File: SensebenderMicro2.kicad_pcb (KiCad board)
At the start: 2 copper layers, 18.7 x 30.5 mm, 31 parts, among them P1 Debug, P2 MYSX_1.2, P3 Antenna, U1 ATSAMD21E, U2 AP1117D33, U3 NRF24L01, U4 RFM69HW, U5 ATSHA204A, U6 AT25DF512C, U7 Si7021, U8 AT24C32-STUM-T, Y1 32Khz

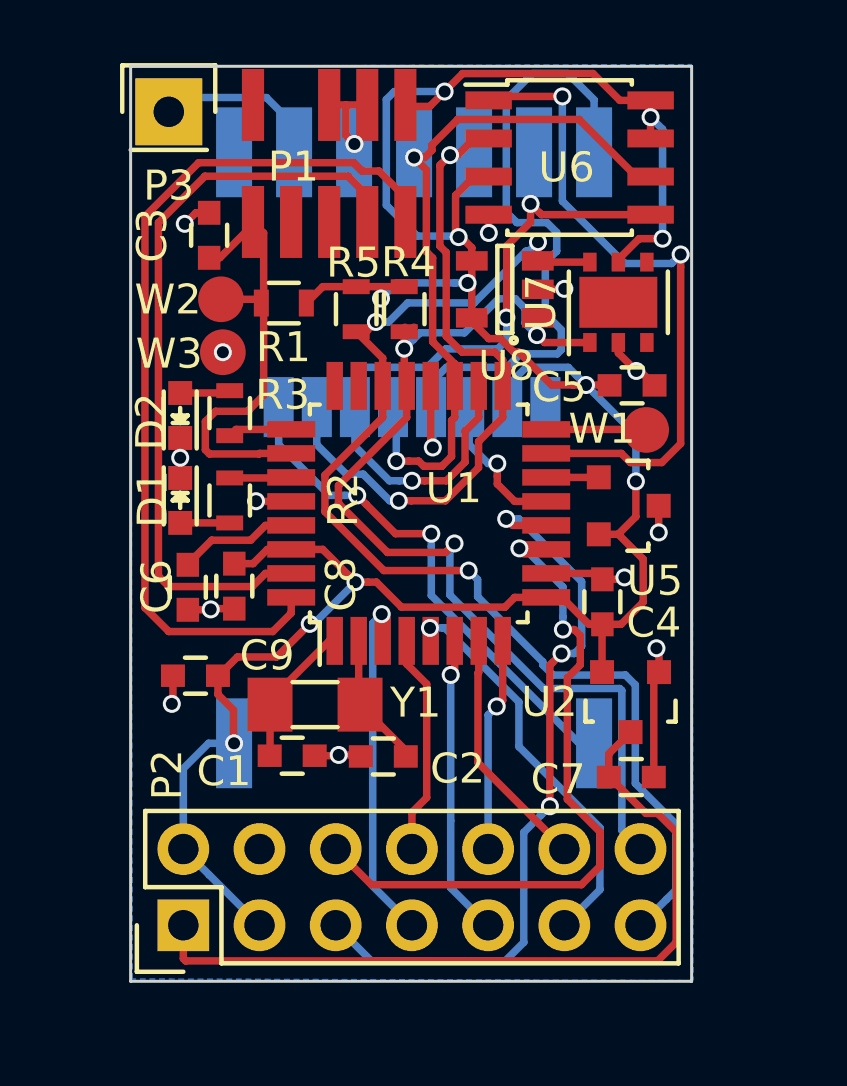
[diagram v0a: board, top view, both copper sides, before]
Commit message: Added filtering for analog supply
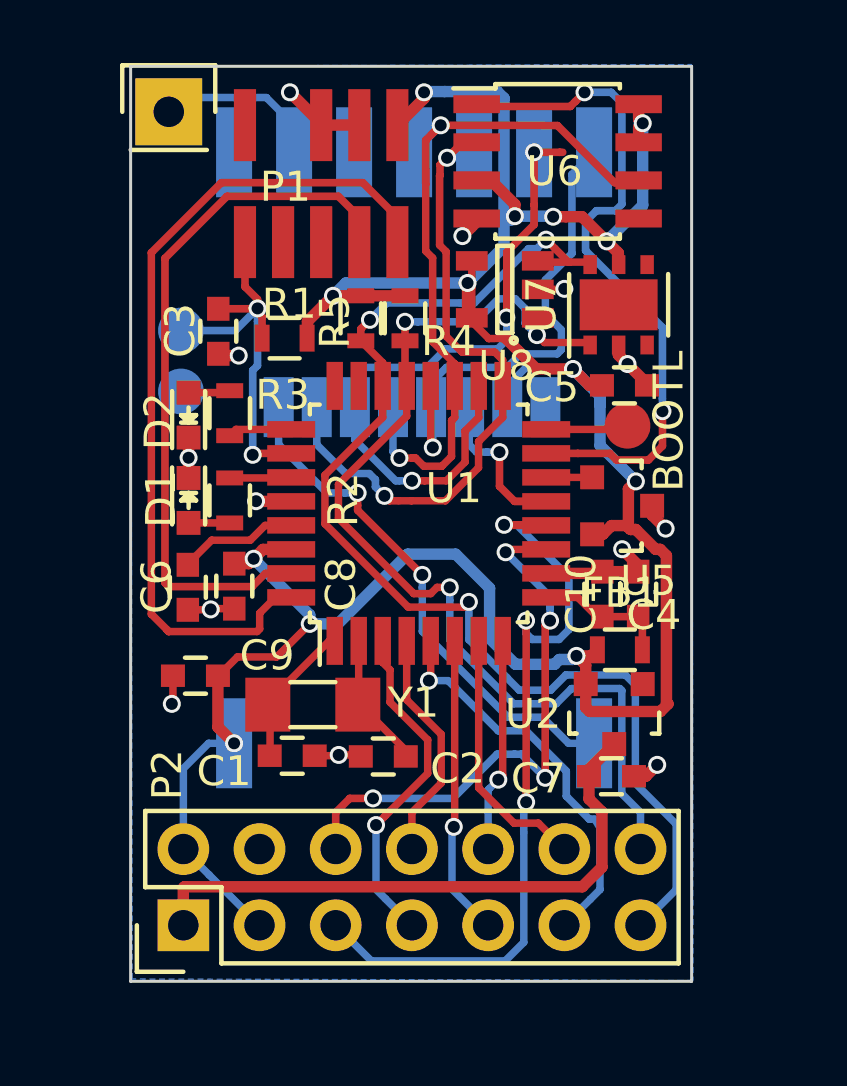
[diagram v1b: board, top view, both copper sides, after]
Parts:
- added C10: CP, Capacitors_SMD:C_0603, F.Cu at (105.9, 99.7)
- added FB1: FILTER, Resistors_SMD:R_0603, F.Cu at (105.3, 101.5)
- added REF**: Symbol_OSHW-Logo_SilkScreen, Symbols:Symbol_OSHW-Logo_SilkScreen, B.Cu at (98.8, 102.5)
- U2: value AP1117D33 -> MCP1703T-3302E
- W2, W3: moved to B.Cu
- moved C3 3.21 mm to (91.9, 90.9), turned to 270 degrees
- moved W3 1.91 mm to (90.7, 92.9)
- moved W2 1.69 mm to (90.7, 90.9)
- moved R1 1.17 mm to (94.1, 91.2)
- moved P1 0.72 mm to (95.4, 86.0)
- moved U2 0.67 mm to (105.1, 103.7)
- moved C7 0.66 mm to (105.0, 105.8)
- moved W1 0.64 mm to (105.6, 94.1)
- moved U6 0.42 mm to (103.2, 85.3)
- moved R5 0.34 mm to (96.7, 90.5)
- moved R4 0.31 mm to (98.1, 90.5)
- moved D2 0.28 mm to (90.9, 93.7)
- moved D1 0.28 mm to (90.9, 96.6)
- moved C4 0.25 mm to (104.7, 99.7)
- moved C5 0.25 mm to (105.5, 92.7)
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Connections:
- net Net-(U4-Pad1) renamed /RFM_RESET
- C4 pad 2: +3V3 -> Net-(C10-Pad1)
- U1 pad 9: +3V3 -> Net-(C10-Pad1)
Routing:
- net /CSN: track 24.5 -> 17.1 mm
- net +3V3: track 89.7 -> 97.0 mm, vias 11 -> 13
- net /V_RAW: track 26.3 -> 20.7 mm
- net Net-(C10-Pad1): track 0.00 -> 4.65 mm
- net /D2_DTM: track 22.8 -> 19.0 mm, vias 2 -> 4
- net /MOSI: track 26.1 -> 23.1 mm
- net /NRF_CE: track 5.00 -> 7.67 mm
- net /D1_DFM: track 24.9 -> 27.0 mm
- net /D7_SCL: track 38.8 -> 40.7 mm
- net /RESET: track 15.6 -> 13.9 mm, vias 0 -> 2
- net /SCK: track 24.1 -> 25.8 mm
- net /SWCLK: track 25.4 -> 23.7 mm
- net /SWDIO: track 29.8 -> 28.3 mm
- net /A1: track 11.9 -> 11.3 mm
- net GND: track 22.2 -> 21.8 mm, vias 14 -> 13
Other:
- net class Default: trace_width 0.25 -> 0.254
- net class power added: clearance 0.2, trace_width 0.381, via_dia 0.6, via_drill 0.4

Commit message: Added fet to switch power to radio / ATSHA
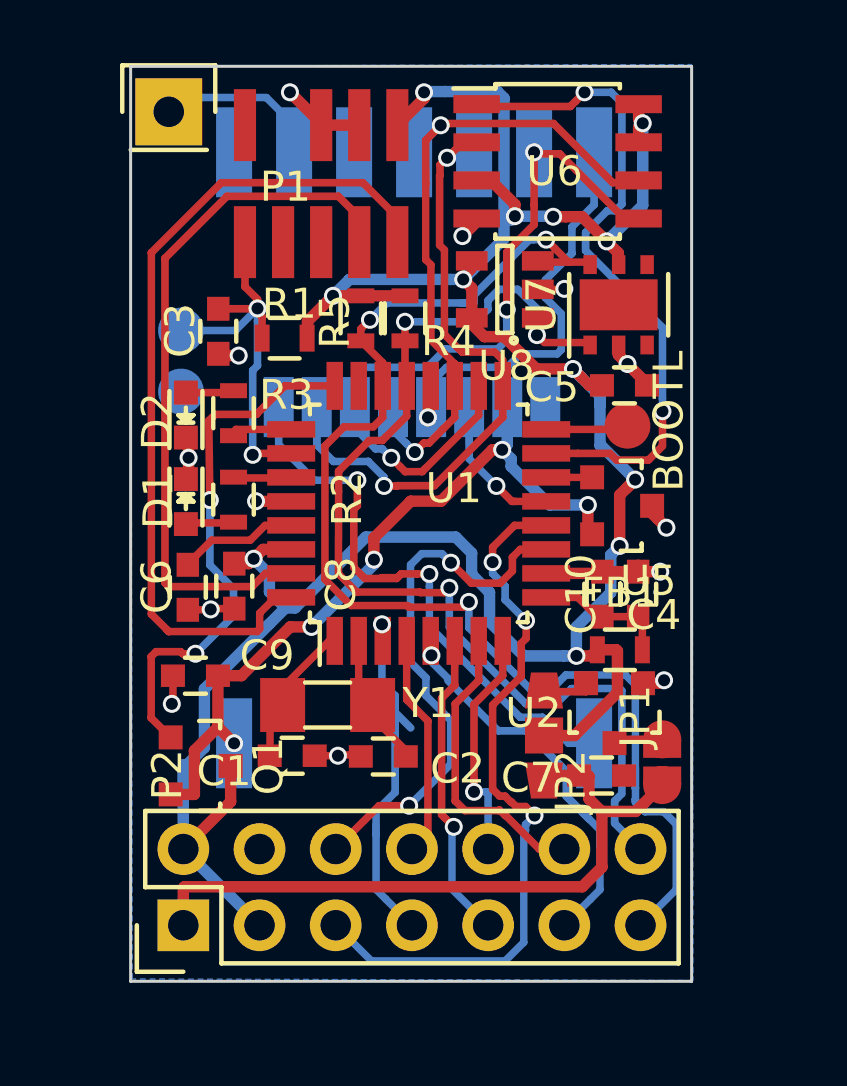
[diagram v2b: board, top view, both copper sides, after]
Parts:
- added JP1: PWR SELECT, mysensors_obscurities:3_pin_solder_jumper_smd, F.Cu at (102.8, 104.4)
- added JP2: JUMPER, mysensors_obscurities:2_pin_solder_jumper_smd, F.Cu at (106.7, 105.3)
- added Q1: Q_NMOS_DGS, TO_SOT_Packages_SMD:SOT-23, F.Cu at (91.3, 105.4)
- C10: value CP -> 10uF
- C7: value C -> 100nF
- U6: value AT25DF512C -> AT45DB041E
- moved Y1 0.49 mm to (95.6, 103.4)
- moved C7 0.33 mm to (104.7, 105.7)
- moved R2 0.13 mm to (92.4, 96.5)
- moved R3 0.13 mm to (92.4, 93.7)
- moved D1 0.10 mm to (90.8, 96.6)
- moved D2 0.09 mm to (90.8, 93.7)
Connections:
- C8 pad 1: +3V3 -> Net-(C8-Pad1)
- C9 pad 2: +3V3 -> +3.3VP
- U2 pad 2: +3V3 -> Net-(C8-Pad1)
- U2 pad 3: /V_RAW -> Net-(JP2-Pad2)
- U3 pad 2: +3V3 -> +3.3VP
- U4 pad 8: +3V3 -> +3.3VP
- U5 pad 2: +3V3 -> +3.3VP
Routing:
- net +3.3VP: track 0.00 -> 26.0 mm, vias 0 -> 5
- net Net-(Q1-Pad1): track 0.00 -> 17.9 mm, vias 0 -> 2
- net +3V3: track 97.0 -> 92.8 mm, vias 13 -> 12
- net /D1_DFM: track 27.0 -> 24.2 mm
- net /V_RAW: track 20.7 -> 23.0 mm
- net /MOSI: track 23.1 -> 25.3 mm
- net /IRQ: track 17.3 -> 19.4 mm
- net Net-(C8-Pad1): track 0.00 -> 2.05 mm
- net /D7_SCL: track 40.7 -> 42.6 mm
- net /D8_SDA: track 34.4 -> 36.4 mm
- net /CSN: track 17.1 -> 15.2 mm
- net /A1: track 11.3 -> 13.2 mm
- net Net-(JP2-Pad2): track 0.00 -> 1.64 mm
- net /NRF_CE: track 7.67 -> 6.13 mm
- net /SCK: track 25.8 -> 24.3 mm
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
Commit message: Added Gate pull up and series resistor to Q1
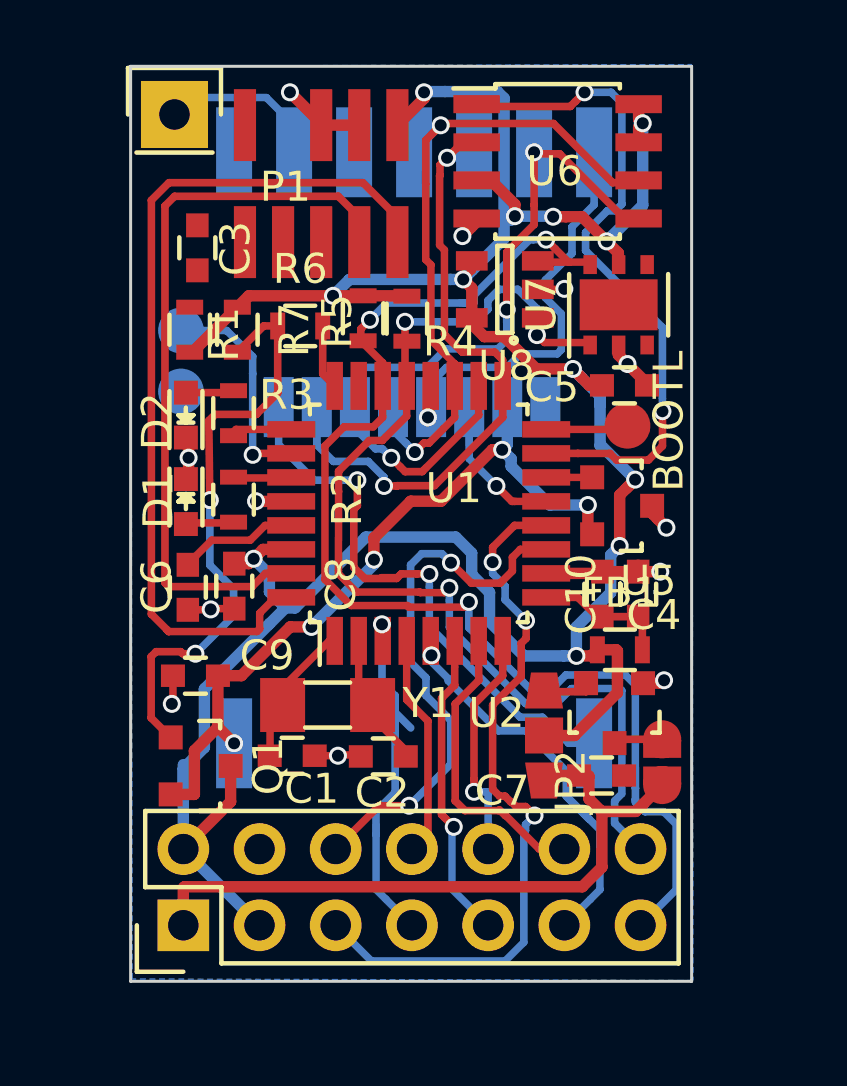
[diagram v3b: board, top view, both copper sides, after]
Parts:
- added R6: 150R, Resistors_SMD:R_0603, F.Cu at (94.7, 90.8)
- added R7: 100K, Resistors_SMD:R_0603, F.Cu at (92.6, 90.9)
- moved R1 3.17 mm to (91.0, 90.9), turned to 90 degrees
- moved C3 2.87 mm to (91.2, 88.2), turned to 90 degrees
- moved P3 0.21 mm to (90.5, 83.7)
- moved R5 0.08 mm to (96.7, 90.5)
- moved R4 0.06 mm to (98.2, 90.5)
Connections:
- U1 pad 24: Net-(Q1-Pad1) -> Net-(R6-Pad2)
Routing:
- net /RESET: track 13.9 -> 7.33 mm, vias 2 -> 1
- net +3V3: track 92.8 -> 96.6 mm
- net Net-(R6-Pad2): track 0.00 -> 2.16 mm
- net Net-(Q1-Pad1): track 17.9 -> 19.9 mm
- net /SWCLK: track 23.7 -> 24.7 mm
- net /SWDIO: track 28.3 -> 29.3 mm
- net GND: track 21.6 -> 20.9 mm, vias 13 -> 12

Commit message: Rerouted to make room for GND via at C7
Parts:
- Q1: value Q_NMOS_DGS -> SI2333DDS-T1-GE3
- R6: value 150R -> 100R
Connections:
- C8 pad 1: Net-(C8-Pad1) -> +3V3
- JP1 pad 1: Net-(C8-Pad1) -> Net-(JP1-Pad1)
- U2 pad 2: Net-(C8-Pad1) -> Net-(JP1-Pad1)
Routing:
- net /RESET: track 7.33 -> 13.0 mm, vias 1 -> 2
- net /D7_SCL: track 42.6 -> 37.4 mm
- net /A1: track 13.2 -> 17.1 mm
- net /V_RAW: track 23.0 -> 26.7 mm
- net /D8_SDA: track 36.4 -> 33.2 mm
- net Net-(C8-Pad1): track 2.05 -> 0.00 mm
- net +3V3: track 96.6 -> 98.6 mm
- net /D5_PWM: track 14.9 -> 13.3 mm
- net Net-(JP1-Pad1): track 0.00 -> 1.57 mm
- net /D2_DTM: track 18.1 -> 16.5 mm
- net /IRQ: track 19.4 -> 18.0 mm
- net /D1_DFM: track 24.2 -> 25.5 mm
- net GND: track 20.9 -> 21.7 mm, vias 12 -> 13
- net +3.3VP: track 26.0 -> 25.5 mm

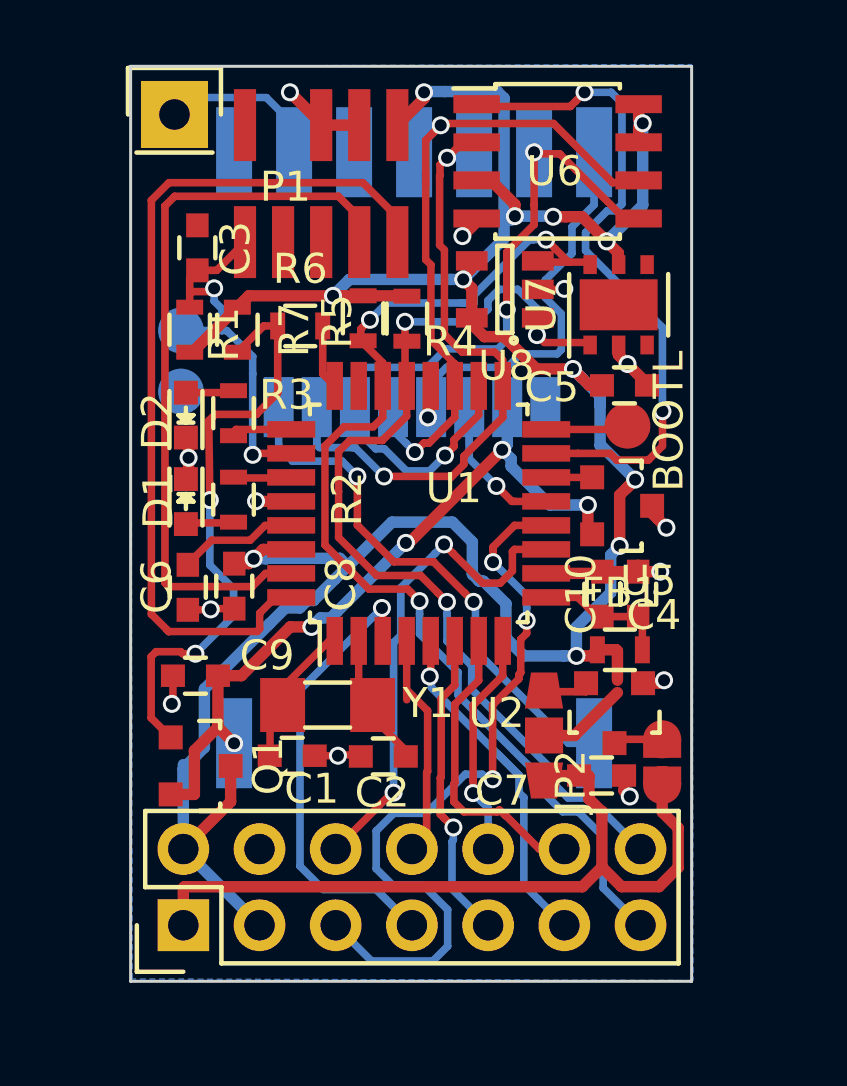
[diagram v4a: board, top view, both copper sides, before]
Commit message: added reset / DIO5 connections to RFM69
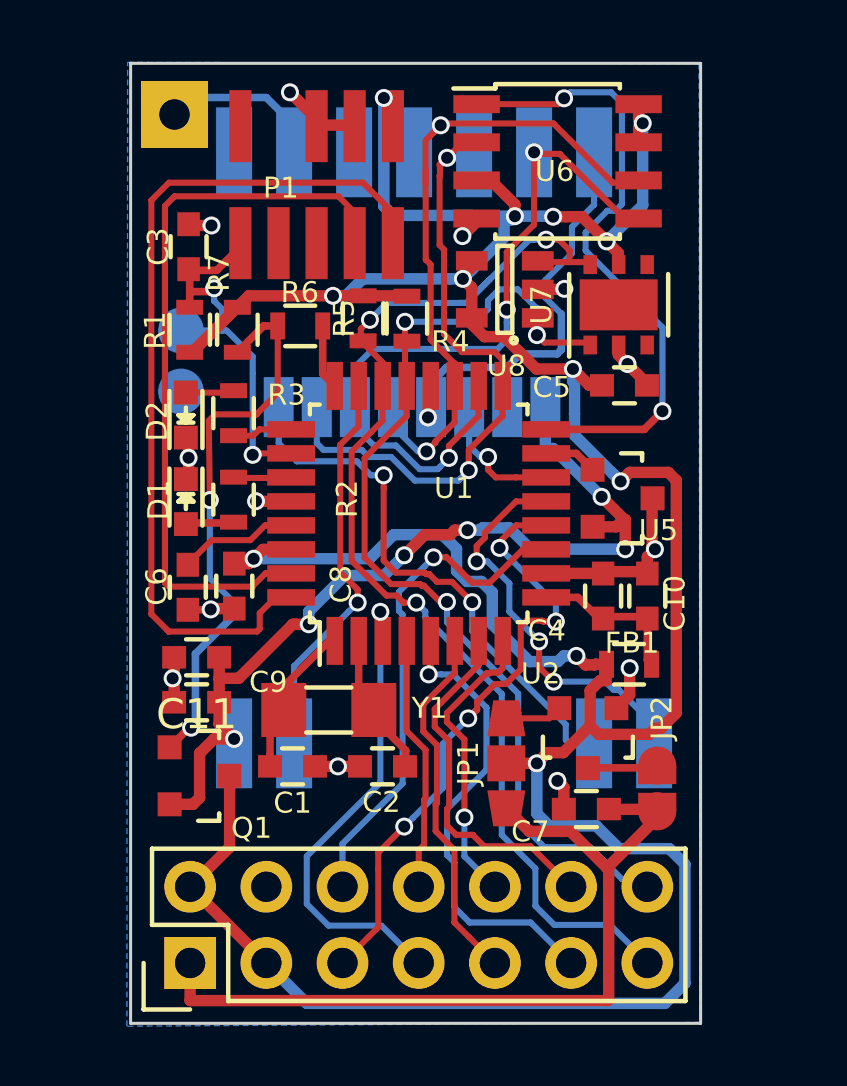
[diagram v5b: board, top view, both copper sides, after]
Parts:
- removed W1: BOOTL, Measurement_Points:Measurement_Point_Round-SMD-Pad_Small
- added C11: 4,7uF, Capacitors_SMD:C_0603, F.Cu at (91.2, 101.8)
- P3: moved to B.Cu
- moved JP1 1.56 mm to (101.5, 105.3)
- moved P2 1.28 mm to (91.0, 112.0)
- moved C7 1.23 mm to (104.2, 106.9), turned to 180 degrees
- moved U2 1.22 mm to (104.2, 104.5)
- moved JP2 0.89 mm to (106.6, 106.2)
- moved C9 0.89 mm to (91.2, 103.3)
- moved FB1 0.57 mm to (105.6, 102.0)
- moved C1 0.36 mm to (94.4, 105.4)
- moved Q1 0.33 mm to (91.3, 105.8)
- moved C2 0.33 mm to (97.4, 105.4)
- moved C10 0.31 mm to (106.2, 99.8)
- moved C3 0.29 mm to (90.9, 88.1)
- moved U5 0.25 mm to (105.4, 96.5)
- moved Y1 0.17 mm to (95.6, 103.6)
- moved P1 0.16 mm to (95.2, 86.0)
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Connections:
- U1 pad 13: /NRF_CE -> /RFM_RESET
- U1 pad 14: /SECURITY -> /NRF_CE
- U1 pad 15: /FLS_CS -> /SECURITY
- U1 pad 16: /BOOTMODE -> /FLS_CS
- U1 pad 23: Net-(U1-Pad23) -> /RFM_DIO5
- U4 pad 7: Net-(U4-Pad7) -> /RFM_DIO5
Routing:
- net +3V3: track 98.6 -> 119.5 mm
- net /RFM_RESET: track 0.00 -> 13.4 mm, vias 0 -> 3
- net /RFM_DIO5: track 0.00 -> 13.3 mm, vias 0 -> 1
- net +3.3VP: track 25.5 -> 30.2 mm, vias 5 -> 6
- net /D1_DFM: track 25.5 -> 20.9 mm, vias 3 -> 4
- net /D5_PWM: track 13.3 -> 16.7 mm
- net /BOOTMODE: track 3.34 -> 0.00 mm
- net GND: track 21.7 -> 24.9 mm
- net /D4_INT: track 7.56 -> 9.87 mm
- net /MISO: track 23.6 -> 21.6 mm
- net /D6_PWM: track 10.1 -> 12.0 mm
- net /D3_INT: track 10.4 -> 12.2 mm, vias 1 -> 0
- net /V_RAW: track 26.7 -> 28.4 mm
- net /NRF_CE: track 6.13 -> 4.54 mm
- net /D7_SCL: track 37.4 -> 38.7 mm
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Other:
- board size 18.7 x 30.5 mm -> 19 x 32 mm
- net class Default: clearance 0.2 -> 0.1778; trace_width 0.254 -> 0.2032
- net class power: clearance 0.2 -> 0.1778
- rule trace_clearance: 0.2 -> 0.1778
- rule trace_min: 0.2 -> 0.1778
